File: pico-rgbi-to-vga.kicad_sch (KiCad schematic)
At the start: 3 parts

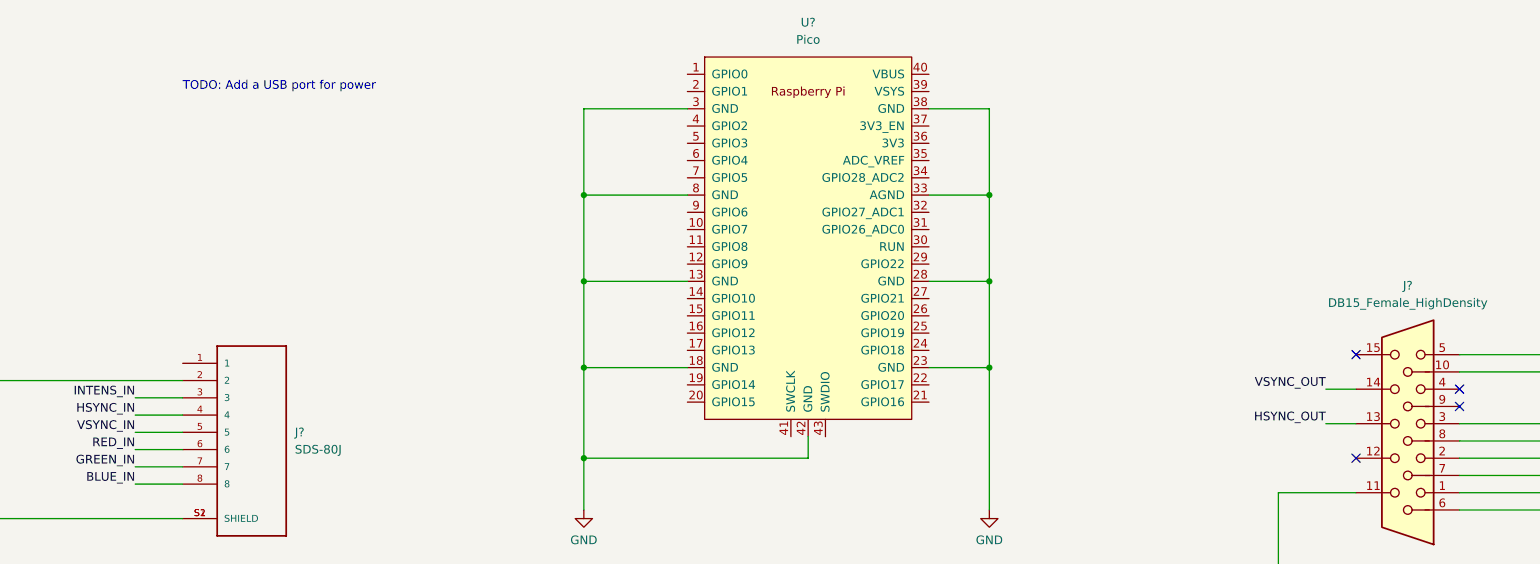
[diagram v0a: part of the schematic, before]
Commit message: Ground plane, bigger board
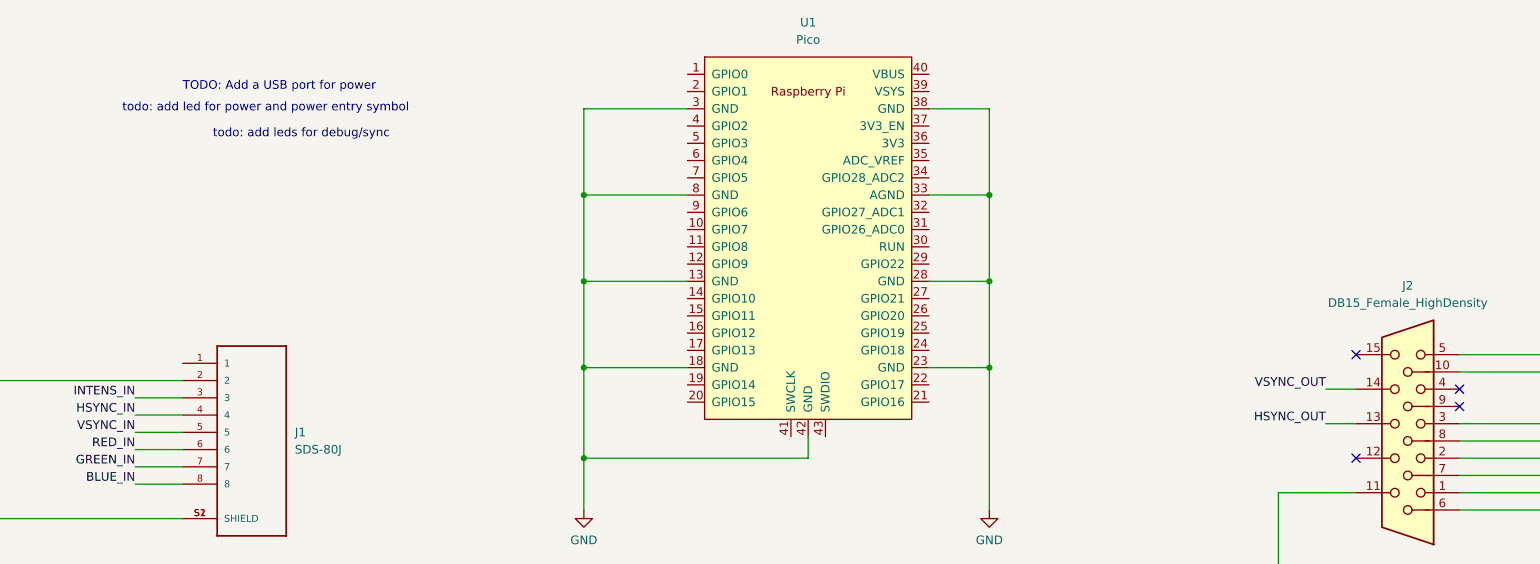
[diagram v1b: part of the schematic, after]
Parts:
- gave numbers to parts that had none: 3
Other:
- note added: "todo: add led for power and power entry symbol"
- note added: "todo: add leds for debug/sync"
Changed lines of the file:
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@@
     (stroke (width 0) (type default) (color 0 0 0 0))
   )
+  (text "todo: add led for power and power entry symbol" (at 52.705 52.705 0)
+    (effects (font (size 1.27 1.27)) (justify left bottom))
+  )
   (text "TODO: Add a USB port for power" (at 61.595 49.53 0)
     (effects (font (size 1.27 1.27)) (justify left bottom))
   )
+  (text "todo: add leds for debug/sync" (at 66.04 56.515 0)
+    (effects (font (size 1.27 1.27)) (justify left bottom))
+  )
   (label "BLUE_OUT" (at 271.78 98.425 0)
     (effects (font (size 1.27 1.27)) (justify left bottom))
@@
   (symbol (lib_id "power:GND") (at 32.385 127 0) (unit 1)
     (in_bom yes) (on_board yes) (fields_autoplaced)
-    (property "Reference" "#PWR?" (id 0) (at 32.385 133.35 0)
+    (property "Reference" "#PWR0101" (id 0) (at 32.385 133.35 0)
       (effects (font (size 1.27 1.27)) hide)
     )
@@
   (symbol (lib_id "MCU_RaspberryPi_and_Boards:Pico") (at 153.67 71.12 0) (unit 1)
     (in_bom yes) (on_board yes) (fields_autoplaced)
-    (property "Reference" "U?" (id 0) (at 153.67 39.37 0))
+    (property "Reference" "U1" (id 0) (at 153.67 39.37 0))
     (property "Value" "Pico" (id 1) (at 153.67 41.91 0))
     (property "Footprint" "MCU_RaspberryPi_and_Boards:RPi_Pico_SMD_TH" (id 2) (at 153.67 71.12 90)
@@
   (symbol (lib_id "power:GND") (at 180.34 111.125 0) (unit 1)
     (in_bom yes) (on_board yes) (fields_autoplaced)
-    (property "Reference" "#PWR?" (id 0) (at 180.34 117.475 0)
+    (property "Reference" "#PWR0104" (id 0) (at 180.34 117.475 0)
       (effects (font (size 1.27 1.27)) hide)
     )
@@
   (symbol (lib_id "power:GND") (at 120.65 111.125 0) (unit 1)
     (in_bom yes) (on_board yes) (fields_autoplaced)
-    (property "Reference" "#PWR?" (id 0) (at 120.65 117.475 0)
+    (property "Reference" "#PWR0102" (id 0) (at 120.65 117.475 0)
       (effects (font (size 1.27 1.27)) hide)
     )
@@
   (symbol (lib_id "power:GND") (at 267.335 122.555 0) (unit 1)
     (in_bom yes) (on_board yes) (fields_autoplaced)
-    (property "Reference" "#PWR?" (id 0) (at 267.335 128.905 0)
+    (property "Reference" "#PWR0103" (id 0) (at 267.335 128.905 0)
       (effects (font (size 1.27 1.27)) hide)
     )
@@
   (symbol (lib_id "SDS-80J:SDS-80J") (at 71.755 99.695 0) (unit 1)
     (in_bom yes) (on_board yes) (fields_autoplaced)
-    (property "Reference" "J?" (id 0) (at 78.105 99.6949 0)
+    (property "Reference" "J1" (id 0) (at 78.105 99.6949 0)
       (effects (font (size 1.27 1.27)) (justify left))
     )
@@
   (symbol (lib_id "Connector:DB15_Female_HighDensity") (at 241.935 98.425 180) (unit 1)
     (in_bom yes) (on_board yes) (fields_autoplaced)
-    (property "Reference" "J?" (id 0) (at 241.935 78.105 0))
+    (property "Reference" "J2" (id 0) (at 241.935 78.105 0))
     (property "Value" "DB15_Female_HighDensity" (id 1) (at 241.935 80.645 0))
     (property "Footprint" "Connector_TE_AMP_HD15:FIXED-1-1734530-1" (id 2) (at 266.065 108.585 0)
@@
   (symbol_instances
     (path "/09dab40b-4c30-4b6a-83f4-2a06979960a7"
-      (reference "#PWR?") (unit 1) (value "GND") (footprint "")
+      (reference "#PWR0101") (unit 1) (value "GND") (footprint "")
+    )
+    (path "/bae9b3c3-dbb6-4a67-aa92-517c26191d31"
+      (reference "#PWR0102") (unit 1) (value "GND") (footprint "")
+    )
+    (path "/cd7a15a9-f843-4aa9-994d-dab66dd0ba9e"
+      (reference "#PWR0103") (unit 1) (value "GND") (footprint "")
     )
     (path "/47badd0a-c557-4a0e-b903-01a70d47942c"
-      (reference "#PWR?") (unit 1) (value "GND") (footprint "")
-    )
-    (path "/bae9b3c3-dbb6-4a67-aa92-517c26191d31"
-      (reference "#PWR?") (unit 1) (value "GND") (footprint "")
-    )
-    (path "/cd7a15a9-f843-4aa9-994d-dab66dd0ba9e"
-      (reference "#PWR?") (unit 1) (value "GND") (footprint "")
+      (reference "#PWR0104") (unit 1) (value "GND") (footprint "")
     )
     (path "/d23f40f8-dca0-4250-87fc-b8a809970f90"
-      (reference "J?") (unit 1) (value "SDS-80J") (footprint "CUI_SDS_80J:CUI_SDS-80J")
+      (reference "J1") (unit 1) (value "SDS-80J") (footprint "CUI_SDS_80J:CUI_SDS-80J")
     )
     (path "/f2704d08-d46a-414b-9e2b-9c98bd284573"
-      (reference "J?") (unit 1) (value "DB15_Female_HighDensity") (footprint "Connector_TE_AMP_HD15:FIXED-1-1734530-1")
+      (reference "J2") (unit 1) (value "DB15_Female_HighDensity") (footprint "Connector_TE_AMP_HD15:FIXED-1-1734530-1")
     )
     (path "/2674e903-9fe3-4a69-b6af-9ed5ebc97bf1"
-      (reference "U?") (unit 1) (value "Pico") (footprint "MCU_RaspberryPi_and_Boards:RPi_Pico_SMD_TH")
-    )
-  )
+      (reference "U1") (unit 1) (value "Pico") (footprint "MCU_RaspberryPi_and_Boards:RPi_Pico_SMD_TH")
+    )
+  )

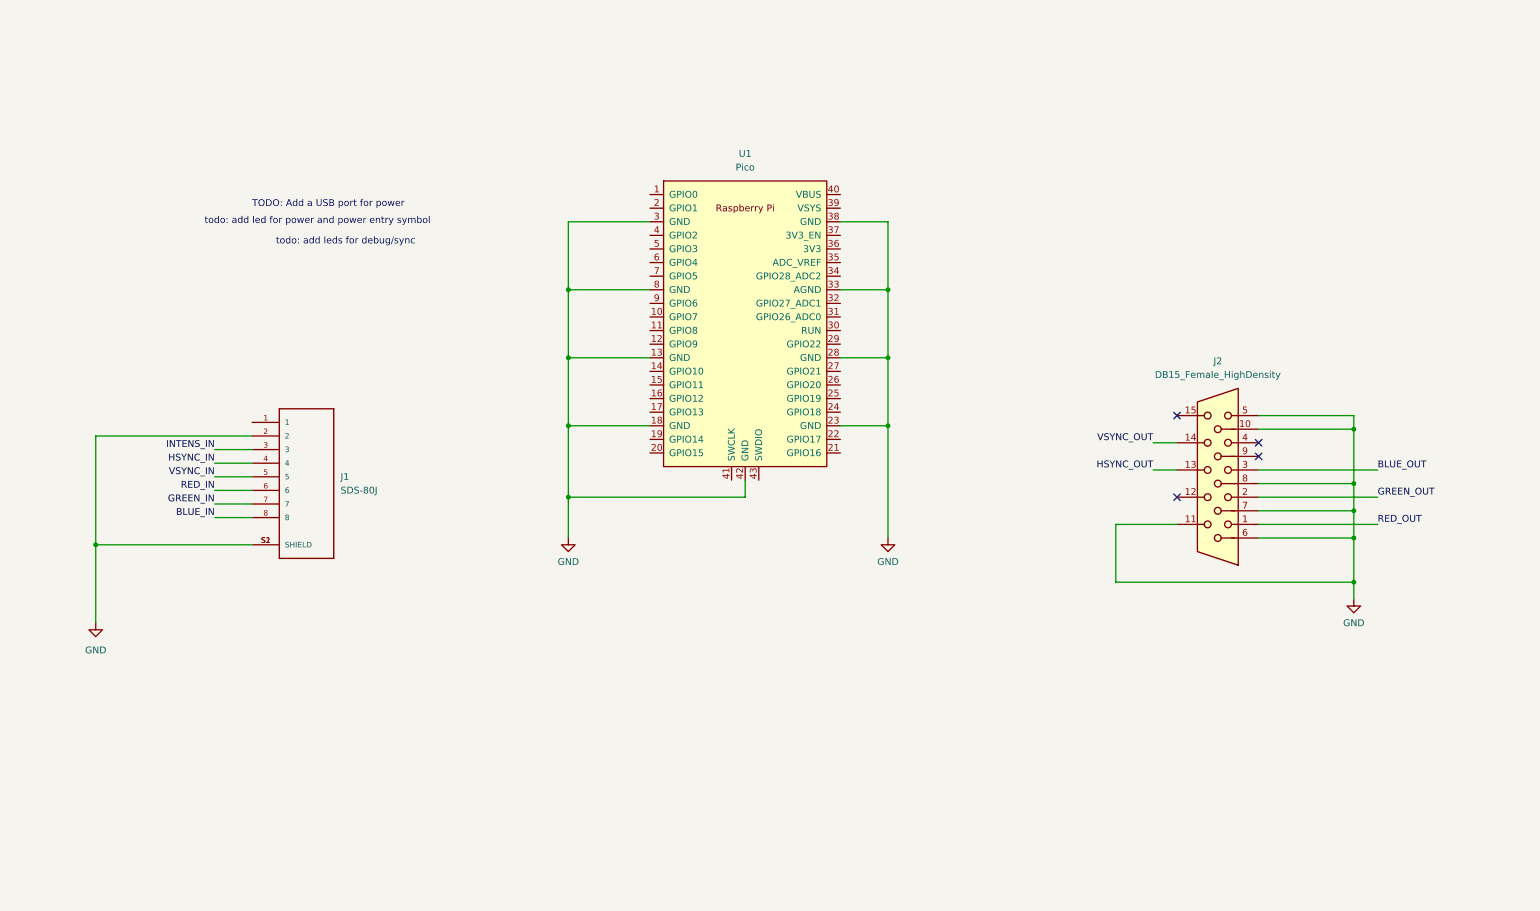
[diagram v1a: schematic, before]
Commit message: Basic left-side implementation with voltage divider
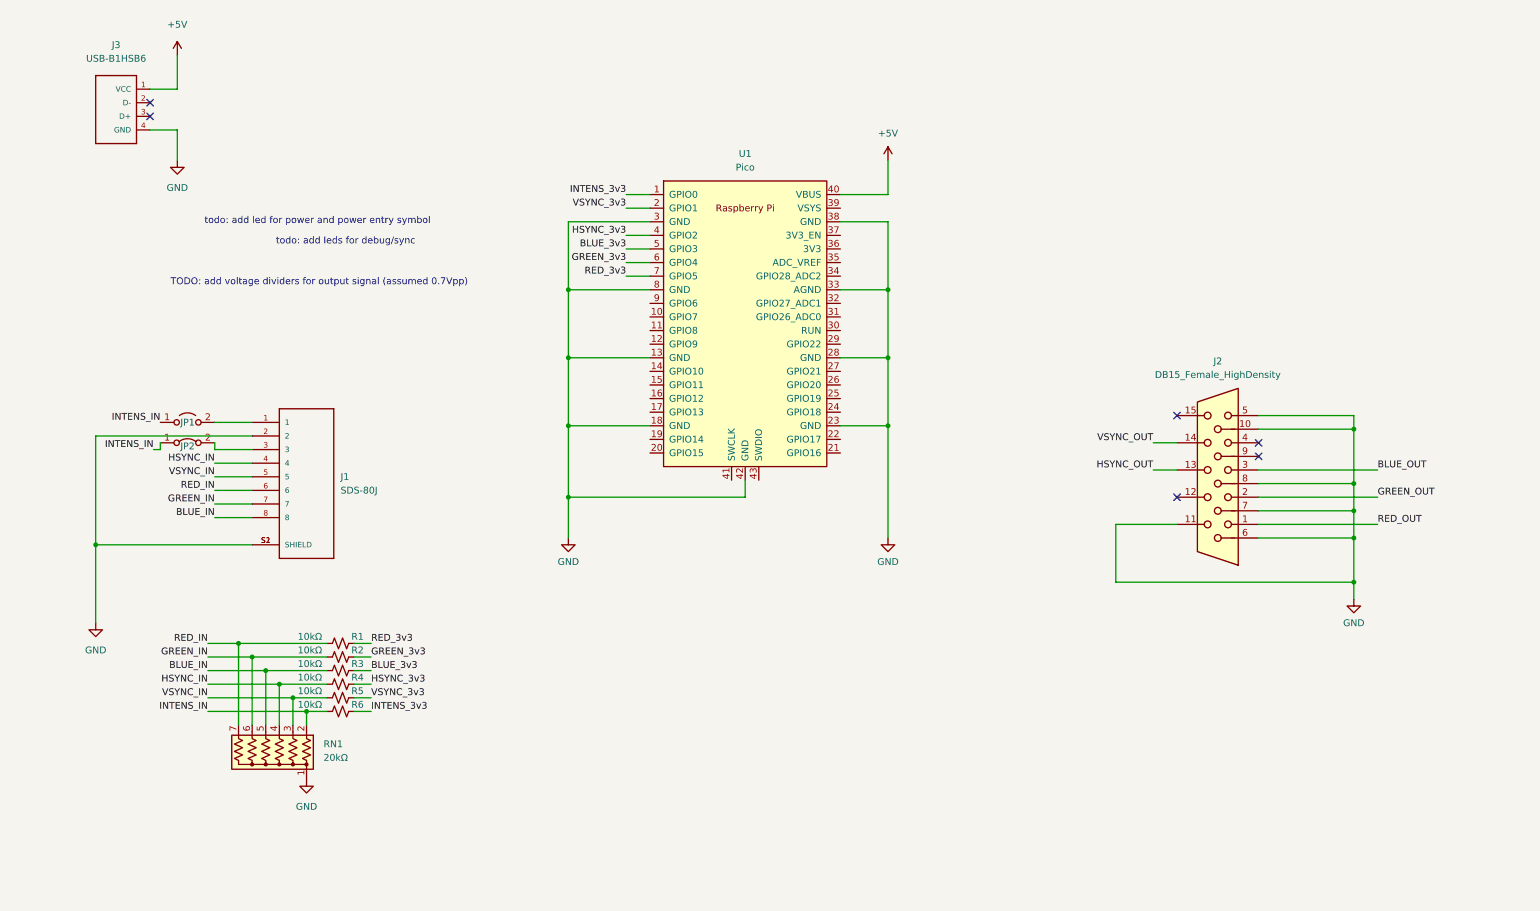
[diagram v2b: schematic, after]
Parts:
- added J3: USB-B1HSB6, USB-B1HSB6:OST_USB-B1HSB6, symbol USB-B1HSB6:USB-B1HSB6
- added JP1: Jumper_2_Open, Jumper:SolderJumper-2_P1.3mm_Open_RoundedPad1.0x1.5mm, symbol Jumper:Jumper_2_Open
- added JP2: Jumper_2_Bridged, Jumper:SolderJumper-2_P1.3mm_Bridged_RoundedPad1.0x1.5mm, symbol Jumper:Jumper_2_Bridged
- added R1, R2, R3, R4, R5, R6: 10kΩ, Resistor_SMD:R_0805_2012Metric_Pad1.20x1.40mm_HandSolder, symbol Device:R_Small_US
- added RN1: 20kΩ, Resistor_THT:R_Array_SIP7, symbol Device:R_Network06_US
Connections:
- net BLUE_IN: now also R3.2, RN1.5 (R4)
- net GND: now also J3.4 (GND), RN1.1 (common)
- net GREEN_IN: now also R2.2, RN1.6 (R5)
- net HSYNC_IN: now also R4.2, RN1.4 (R3)
- net INTENS_IN: now also JP1.1 (A), JP2.1 (A), R6.2, RN1.2 (R1); no longer J1.3
- net RED_IN: now also R1.2, RN1.7 (R6)
- net VSYNC_IN: now also R5.2, RN1.3 (R2)
- net INTENS_3v3: now reaches U1.1 (GPIO0)
- net INTENS_3v3: now also R6.1
- net VSYNC_3v3: now reaches U1.2 (GPIO1)
- net VSYNC_3v3: now also R5.1
- net HSYNC_3v3: now reaches U1.4 (GPIO2)
- net HSYNC_3v3: now also R4.1
- net +5V: now reaches U1.40 (VBUS)
- net +5V: now also J3.1 (VCC)
- net BLUE_3v3: now reaches U1.5 (GPIO3)
- net BLUE_3v3: now also R3.1
- net GREEN_3v3: now reaches U1.6 (GPIO4)
- net GREEN_3v3: now also R2.1
- net RED_3v3: now reaches U1.7 (GPIO5)
- net RED_3v3: now also R1.1
- net at J1.1: now also JP1.2 (B)
- new net: J1.3, JP2.2 (B)
- no-connect marks 4 -> 6
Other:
- note added: "TODO: add voltage dividers for output signal (assumed 0.7Vpp)"
- note removed: "TODO: Add a USB port for power"

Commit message: Power LED, output voltage divider
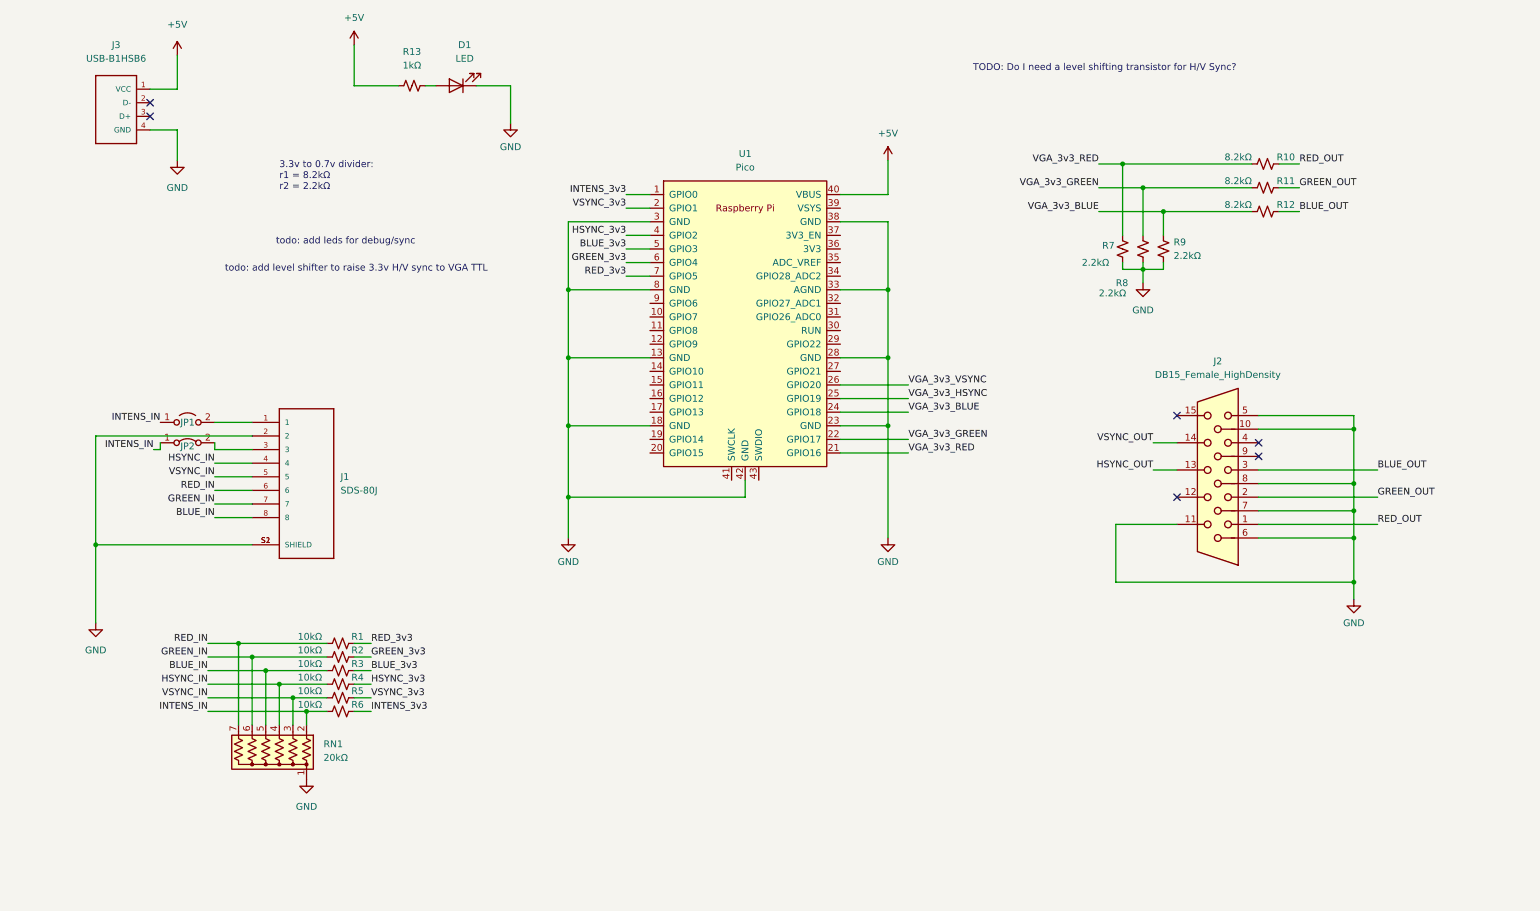
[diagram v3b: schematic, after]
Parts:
- added D1: LED, LED_THT:LED_D3.0mm, symbol Device:LED
- added R10, R11, R12: 8.2kΩ, Resistor_SMD:R_0805_2012Metric_Pad1.20x1.40mm_HandSolder, symbol Device:R_Small_US
- added R13: 1kΩ, Resistor_SMD:R_0805_2012Metric_Pad1.20x1.40mm_HandSolder, symbol Device:R_Small_US
- added R7, R8, R9: 2.2kΩ, Resistor_SMD:R_0805_2012Metric_Pad1.20x1.40mm_HandSolder, symbol Device:R_Small_US
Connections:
- net +5V: now also R13.1
- net BLUE_OUT: now also R12.2
- net GND: now also D1.1 (K), R7.2, R8.2, R9.2
- net GREEN_OUT: now also R11.2
- net RED_OUT: now also R10.2
- net VGA_3v3_RED: now reaches U1.21 (GPIO16)
- net VGA_3v3_RED: now also R10.1, R7.1
- net VGA_3v3_GREEN: now reaches U1.22 (GPIO17)
- net VGA_3v3_GREEN: now also R11.1, R8.1
- net VGA_3v3_BLUE: now reaches U1.24 (GPIO18)
- net VGA_3v3_BLUE: now also R12.1, R9.1
- net VGA_3v3_HSYNC: now reaches U1.25 (GPIO19)
- net VGA_3v3_VSYNC: now reaches U1.26 (GPIO20)
- new net: D1.2 (A), R13.2
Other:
- note added: "3.3v to 0.7v divider: r1 = 8.2kΩ r2 = 2.2kΩ"
- note added: "TODO: Do I need a level shifting transistor for H/V Sync?"
- note added: "todo: add level shifter to raise 3.3v H/V sync to VGA TTL"
- note removed: "TODO: add voltage dividers for output signal (assumed 0.7Vpp)"
- note removed: "todo: add led for power and power entry symbol"

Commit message: Fully laid out, I think
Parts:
- added Q1, Q2: 2n2222, Package_TO_SOT_THT:TO-92_Inline, symbol Device:Q_NPN_EBC
- added R14, R16: 1kΩ, Resistor_SMD:R_0805_2012Metric_Pad1.20x1.40mm_HandSolder, symbol Device:R_Small_US
- added R15, R17: 10kΩ, Resistor_SMD:R_0805_2012Metric_Pad1.20x1.40mm_HandSolder, symbol Device:R_Small_US
- added SW?: SW_Push, Button_Switch_THT:SW_PUSH_6mm, symbol Switch:SW_Push
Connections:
- net +5V: now also R15.1, R17.1
- net GND: now also SW?.1
- net HSYNC_OUT: now also Q1.3 (C), R15.2
- net VGA_3v3_HSYNC: now also Q1.1 (E)
- net VGA_3v3_VSYNC: now also Q2.1 (E)
- net VSYNC_OUT: now also Q2.3 (C), R17.2
- net SW_PALETTE_CHANGE: now reaches U1.20 (GPIO15)
- net SW_PALETTE_CHANGE: now also SW?.2
- net +3V3: now reaches U1.36 (3V3)
- net +3V3: now also R14.1, R16.1
- new net: Q1.2 (B), R14.2
- new net: Q2.2 (B), R16.2
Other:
- note added: "level shifting for h/v sync (VGA wants TTL level)"
- note removed: "TODO: Do I need a level shifting transistor for H/V Sync?"
- moved on the sheet: J2, R10, R11, R12, R7, R8, R9
